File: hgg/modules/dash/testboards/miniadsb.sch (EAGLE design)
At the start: 16 parts, among them IC1 TLC272D, IC2 LM339D, IC3 7414D

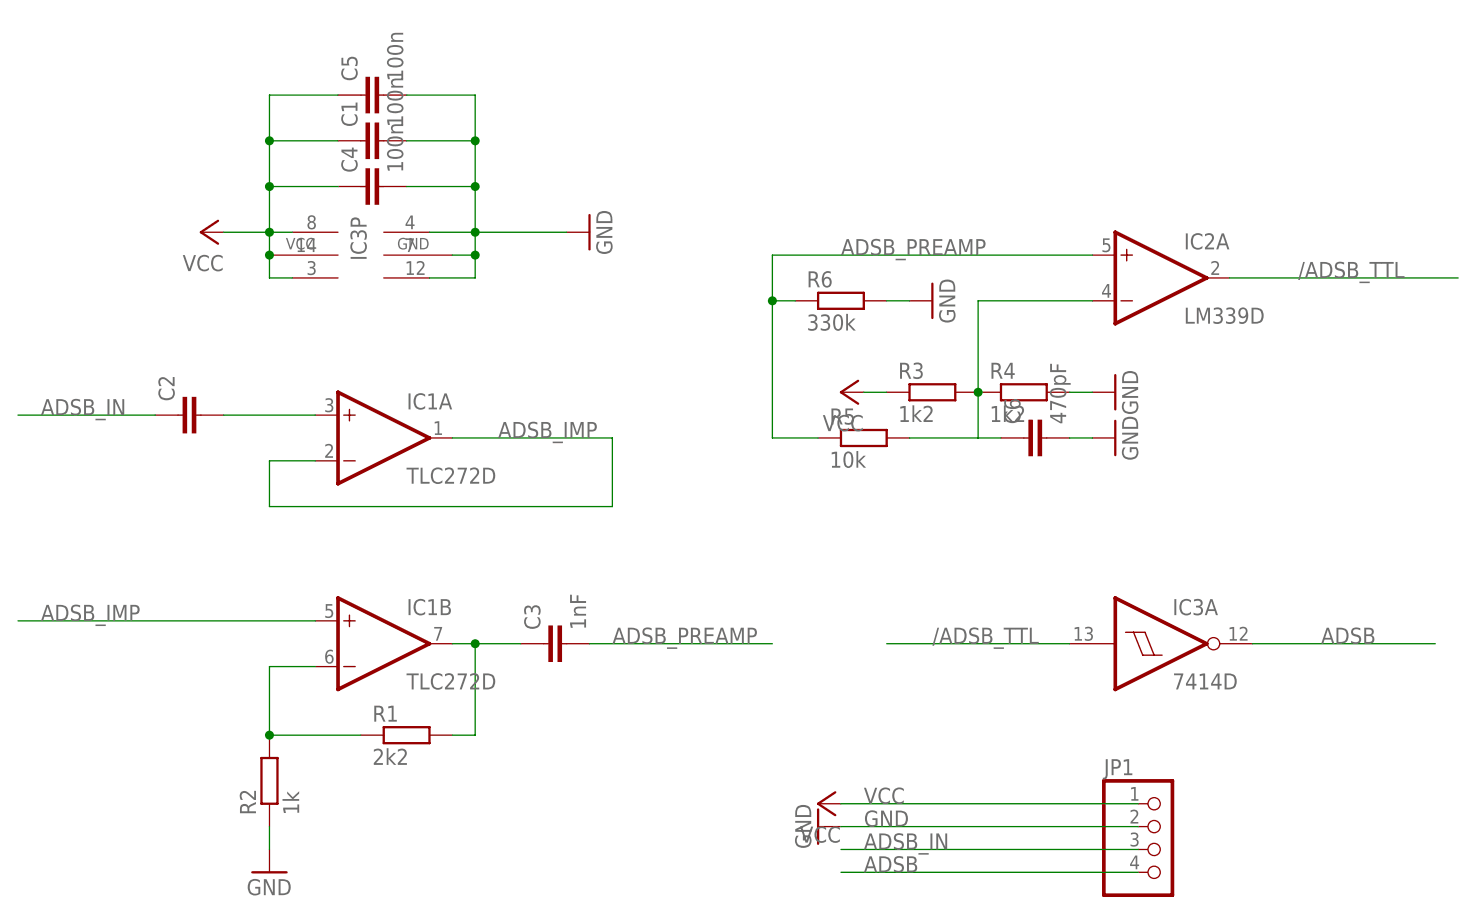
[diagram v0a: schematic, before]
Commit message: changed to use DIL chips
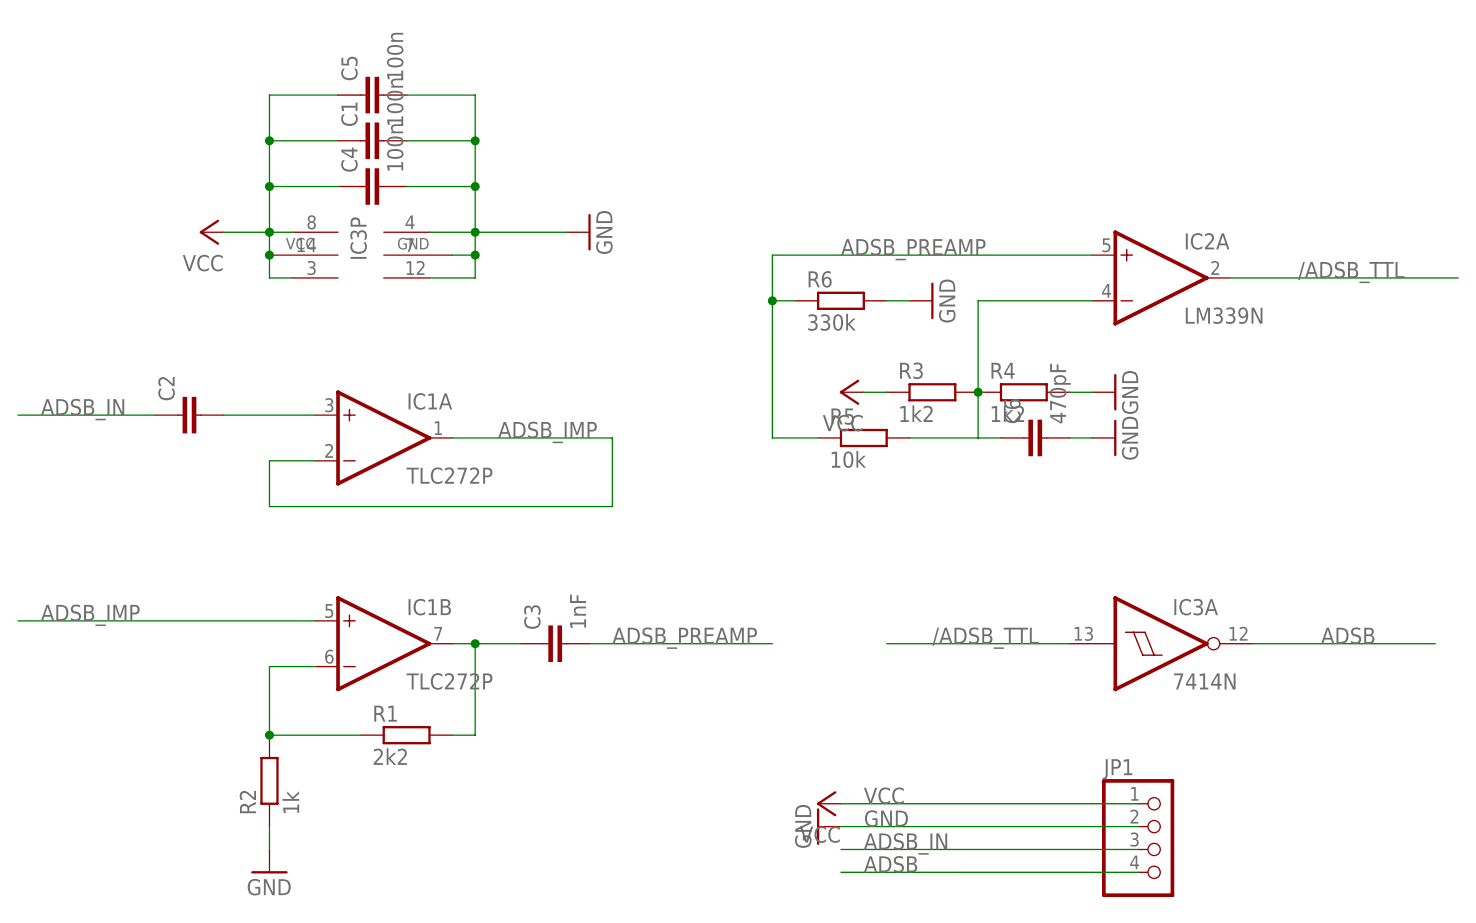
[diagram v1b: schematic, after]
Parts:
- IC1: value TLC272D -> TLC272P; device linear:TLC272D -> linear:TLC272P
- IC2: value LM339D -> LM339N; device linear:LM339D -> linear:LM339N
- IC3: value 7414D -> 7414N; device 74xx-us:7414D -> 74xx-us:7414N
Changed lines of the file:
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@@
 <grid distance="0.1" unitdist="inch" unit="inch" style="lines" multiple="1" display="no" altdistance="0.01" altunitdist="inch" altunit="inch"/>
 <layers>
-<layer number="1" name="Top" color="4" fill="1" visible="no" active="no"/>
-<layer number="16" name="Bottom" color="1" fill="1" visible="no" active="no"/>
-<layer number="17" name="Pads" color="2" fill="1" visible="no" active="no"/>
-<layer number="18" name="Vias" color="2" fill="1" visible="no" active="no"/>
-<layer number="19" name="Unrouted" color="6" fill="1" visible="no" active="no"/>
-<layer number="20" name="Dimension" color="15" fill="1" visible="no" active="no"/>
-<layer number="21" name="tPlace" color="7" fill="1" visible="no" active="no"/>
-<layer number="22" name="bPlace" color="7" fill="1" visible="no" active="no"/>
-<layer number="23" name="tOrigins" color="15" fill="1" visible="no" active="no"/>
-<layer number="24" name="bOrigins" color="15" fill="1" visible="no" active="no"/>
-<layer number="25" name="tNames" color="7" fill="1" visible="no" active="no"/>
-<layer number="26" name="bNames" color="7" fill="1" visible="no" active="no"/>
-<layer number="27" name="tValues" color="7" fill="1" visible="no" active="no"/>
-<layer number="28" name="bValues" color="7" fill="1" visible="no" active="no"/>
+<layer number="1" name="Top" color="4" fill="1" visible="yes" active="no"/>
+<layer number="16" name="Bottom" color="1" fill="1" visible="yes" active="no"/>
+<layer number="17" name="Pads" color="2" fill="1" visible="yes" active="no"/>
+<layer number="18" name="Vias" color="2" fill="1" visible="yes" active="no"/>
+<layer number="19" name="Unrouted" color="6" fill="1" visible="yes" active="no"/>
+<layer number="20" name="Dimension" color="15" fill="1" visible="yes" active="no"/>
+<layer number="21" name="tPlace" color="7" fill="1" visible="yes" active="no"/>
+<layer number="22" name="bPlace" color="7" fill="1" visible="yes" active="no"/>
+<layer number="23" name="tOrigins" color="15" fill="1" visible="yes" active="no"/>
+<layer number="24" name="bOrigins" color="15" fill="1" visible="yes" active="no"/>
+<layer number="25" name="tNames" color="7" fill="1" visible="yes" active="no"/>
+<layer number="26" name="bNames" color="7" fill="1" visible="yes" active="no"/>
+<layer number="27" name="tValues" color="7" fill="1" visible="yes" active="no"/>
+<layer number="28" name="bValues" color="7" fill="1" visible="yes" active="no"/>
 <layer number="29" name="tStop" color="7" fill="3" visible="no" active="no"/>
 <layer number="30" name="bStop" color="7" fill="6" visible="no" active="no"/>
@@
 <layer number="35" name="tGlue" color="7" fill="4" visible="no" active="no"/>
 <layer number="36" name="bGlue" color="7" fill="5" visible="no" active="no"/>
-<layer number="37" name="tTest" color="7" fill="1" visible="no" active="no"/>
-<layer number="38" name="bTest" color="7" fill="1" visible="no" active="no"/>
+<layer number="37" name="tTest" color="7" fill="1" visible="yes" active="no"/>
+<layer number="38" name="bTest" color="7" fill="1" visible="yes" active="no"/>
 <layer number="39" name="tKeepout" color="4" fill="11" visible="no" active="no"/>
 <layer number="40" name="bKeepout" color="1" fill="11" visible="no" active="no"/>
@@
 <layer number="44" name="Drills" color="7" fill="1" visible="no" active="no"/>
 <layer number="45" name="Holes" color="7" fill="1" visible="no" active="no"/>
-<layer number="46" name="Milling" color="3" fill="1" visible="no" active="no"/>
-<layer number="47" name="Measures" color="7" fill="1" visible="no" active="no"/>
-<layer number="48" name="Document" color="7" fill="1" visible="no" active="no"/>
-<layer number="49" name="Reference" color="7" fill="1" visible="no" active="no"/>
-<layer number="51" name="tDocu" color="6" fill="1" visible="no" active="no"/>
-<layer number="52" name="bDocu" color="7" fill="1" visible="no" active="no"/>
+<layer number="46" name="Milling" color="3" fill="1" visible="yes" active="no"/>
+<layer number="47" name="Measures" color="7" fill="1" visible="yes" active="no"/>
+<layer number="48" name="Document" color="7" fill="1" visible="yes" active="no"/>
+<layer number="49" name="Reference" color="7" fill="1" visible="yes" active="no"/>
+<layer number="51" name="tDocu" color="7" fill="1" visible="yes" active="no"/>
+<layer number="52" name="bDocu" color="7" fill="1" visible="yes" active="no"/>
 <layer number="91" name="Nets" color="2" fill="1" visible="yes" active="yes"/>
 <layer number="92" name="Busses" color="1" fill="1" visible="yes" active="yes"/>
@@
 </classes>
 <parts>
-<part name="IC1" library="linear" deviceset="TLC272" device="D"/>
+<part name="IC1" library="linear" deviceset="TLC272" device="P"/>
 <part name="GND1" library="supply1" deviceset="GND" device=""/>
 <part name="P+1" library="supply1" deviceset="VCC" device=""/>
@@
 <part name="GND2" library="supply1" deviceset="GND" device=""/>
 <part name="C3" library="resistor" deviceset="C-EU" device="C0805" value="1nF"/>
-<part name="IC2" library="linear" deviceset="LM339" device="D"/>
-<part name="IC3" library="74xx-us" deviceset="74*14" device="D"/>
+<part name="IC2" library="linear" deviceset="LM339" device="N"/>
+<part name="IC3" library="74xx-us" deviceset="74*14" device="N"/>
 <part name="C4" library="resistor" deviceset="C-EU" device="C0805" value="100n"/>
 <part name="C5" library="resistor" deviceset="C-EU" device="C0805" value="100n"/>

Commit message: updates
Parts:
- added R7: 1k, rcl:R-EU_R0603
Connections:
- net /ADSB_TTL: now also R7.1
- net VCC: now also R7.2
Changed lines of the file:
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@@
 <grid distance="0.1" unitdist="inch" unit="inch" style="lines" multiple="1" display="no" altdistance="0.01" altunitdist="inch" altunit="inch"/>
 <layers>
-<layer number="1" name="Top" color="4" fill="1" visible="yes" active="no"/>
-<layer number="16" name="Bottom" color="1" fill="1" visible="yes" active="no"/>
-<layer number="17" name="Pads" color="2" fill="1" visible="yes" active="no"/>
-<layer number="18" name="Vias" color="2" fill="1" visible="yes" active="no"/>
-<layer number="19" name="Unrouted" color="6" fill="1" visible="yes" active="no"/>
-<layer number="20" name="Dimension" color="15" fill="1" visible="yes" active="no"/>
-<layer number="21" name="tPlace" color="7" fill="1" visible="yes" active="no"/>
-<layer number="22" name="bPlace" color="7" fill="1" visible="yes" active="no"/>
-<layer number="23" name="tOrigins" color="15" fill="1" visible="yes" active="no"/>
-<layer number="24" name="bOrigins" color="15" fill="1" visible="yes" active="no"/>
-<layer number="25" name="tNames" color="7" fill="1" visible="yes" active="no"/>
-<layer number="26" name="bNames" color="7" fill="1" visible="yes" active="no"/>
-<layer number="27" name="tValues" color="7" fill="1" visible="yes" active="no"/>
-<layer number="28" name="bValues" color="7" fill="1" visible="yes" active="no"/>
+<layer number="1" name="Top" color="4" fill="1" visible="no" active="no"/>
+<layer number="16" name="Bottom" color="1" fill="1" visible="no" active="no"/>
+<layer number="17" name="Pads" color="2" fill="1" visible="no" active="no"/>
+<layer number="18" name="Vias" color="2" fill="1" visible="no" active="no"/>
+<layer number="19" name="Unrouted" color="6" fill="1" visible="no" active="no"/>
+<layer number="20" name="Dimension" color="15" fill="1" visible="no" active="no"/>
+<layer number="21" name="tPlace" color="7" fill="1" visible="no" active="no"/>
+<layer number="22" name="bPlace" color="7" fill="1" visible="no" active="no"/>
+<layer number="23" name="tOrigins" color="15" fill="1" visible="no" active="no"/>
+<layer number="24" name="bOrigins" color="15" fill="1" visible="no" active="no"/>
+<layer number="25" name="tNames" color="7" fill="1" visible="no" active="no"/>
+<layer number="26" name="bNames" color="7" fill="1" visible="no" active="no"/>
+<layer number="27" name="tValues" color="7" fill="1" visible="no" active="no"/>
+<layer number="28" name="bValues" color="7" fill="1" visible="no" active="no"/>
 <layer number="29" name="tStop" color="7" fill="3" visible="no" active="no"/>
 <layer number="30" name="bStop" color="7" fill="6" visible="no" active="no"/>
@@
 <layer number="35" name="tGlue" color="7" fill="4" visible="no" active="no"/>
 <layer number="36" name="bGlue" color="7" fill="5" visible="no" active="no"/>
-<layer number="37" name="tTest" color="7" fill="1" visible="yes" active="no"/>
-<layer number="38" name="bTest" color="7" fill="1" visible="yes" active="no"/>
+<layer number="37" name="tTest" color="7" fill="1" visible="no" active="no"/>
+<layer number="38" name="bTest" color="7" fill="1" visible="no" active="no"/>
 <layer number="39" name="tKeepout" color="4" fill="11" visible="no" active="no"/>
 <layer number="40" name="bKeepout" color="1" fill="11" visible="no" active="no"/>
@@
 <layer number="44" name="Drills" color="7" fill="1" visible="no" active="no"/>
 <layer number="45" name="Holes" color="7" fill="1" visible="no" active="no"/>
-<layer number="46" name="Milling" color="3" fill="1" visible="yes" active="no"/>
-<layer number="47" name="Measures" color="7" fill="1" visible="yes" active="no"/>
-<layer number="48" name="Document" color="7" fill="1" visible="yes" active="no"/>
-<layer number="49" name="Reference" color="7" fill="1" visible="yes" active="no"/>
-<layer number="51" name="tDocu" color="7" fill="1" visible="yes" active="no"/>
-<layer number="52" name="bDocu" color="7" fill="1" visible="yes" active="no"/>
+<layer number="46" name="Milling" color="3" fill="1" visible="no" active="no"/>
+<layer number="47" name="Measures" color="7" fill="1" visible="no" active="no"/>
+<layer number="48" name="Document" color="7" fill="1" visible="no" active="no"/>
+<layer number="49" name="Reference" color="7" fill="1" visible="no" active="no"/>
+<layer number="51" name="tDocu" color="7" fill="1" visible="no" active="no"/>
+<layer number="52" name="bDocu" color="7" fill="1" visible="no" active="no"/>
 <layer number="91" name="Nets" color="2" fill="1" visible="yes" active="yes"/>
 <layer number="92" name="Busses" color="1" fill="1" visible="yes" active="yes"/>
@@
 <part name="P+3" library="supply1" deviceset="VCC" device=""/>
 <part name="GND6" library="supply1" deviceset="GND" device=""/>
+<part name="P+4" library="supply1" deviceset="VCC" device=""/>
+<part name="R7" library="rcl" deviceset="R-EU_" device="R0603" value="1k"/>
 </parts>
 <sheets>
@@
 <instance part="P+3" gate="VCC" x="104.14" y="22.86" rot="R90"/>
 <instance part="GND6" gate="1" x="104.14" y="20.32" rot="R270"/>
+<instance part="P+4" gate="VCC" x="154.94" y="99.06"/>
+<instance part="R7" gate="G$1" x="154.94" y="88.9" rot="R90"/>
 </instances>
 <busses>
@@
 <pinref part="P+3" gate="VCC" pin="VCC"/>
 </segment>
+<segment>
+<pinref part="P+4" gate="VCC" pin="VCC"/>
+<pinref part="R7" gate="G$1" pin="2"/>
+<wire x1="154.94" y1="93.98" x2="154.94" y2="96.52" width="0.1524" layer="91"/>
+</segment>
 </net>
 <net name="N$1" class="0">
@@
 <segment>
 <pinref part="IC2" gate="A" pin="OUT"/>
-<wire x1="149.86" y1="81.28" x2="175.26" y2="81.28" width="0.1524" layer="91"/>
+<wire x1="149.86" y1="81.28" x2="154.94" y2="81.28" width="0.1524" layer="91"/>
 <label x="157.48" y="81.28" size="1.778" layer="95"/>
-</segment>
-<segment>
+<pinref part="R7" gate="G$1" pin="1"/>
+<wire x1="154.94" y1="81.28" x2="175.26" y2="81.28" width="0.1524" layer="91"/>
+<wire x1="154.94" y1="83.82" x2="154.94" y2="81.28" width="0.1524" layer="91"/>
+<junction x="154.94" y="81.28"/>
+</segment>
+<segment>
